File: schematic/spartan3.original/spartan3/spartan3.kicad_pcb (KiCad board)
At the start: 2 copper layers, 215.9 x 160 mm, 283 parts, among them U1_clk_select_0 SPFT_Sliding_Switch-dynacore, U2 XC3S250E-4TQG144C

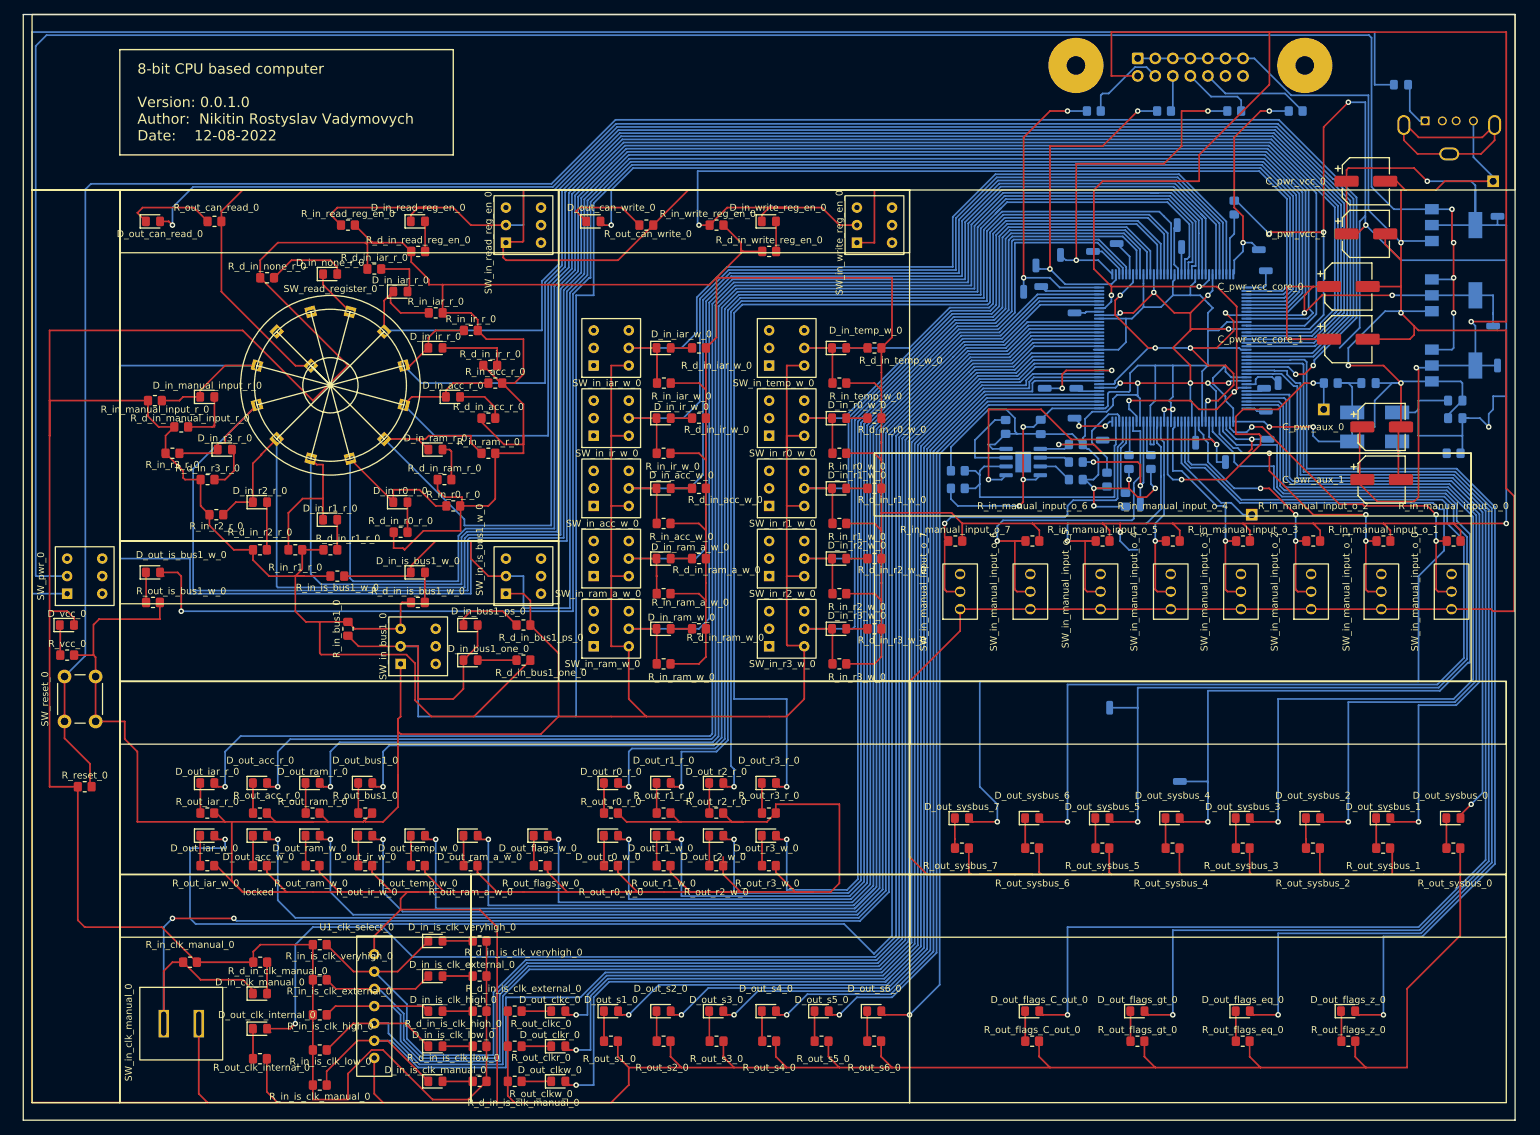
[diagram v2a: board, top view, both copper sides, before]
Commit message: Schematics/PCB layout updated. Gerber/Drill/BOM re-generated
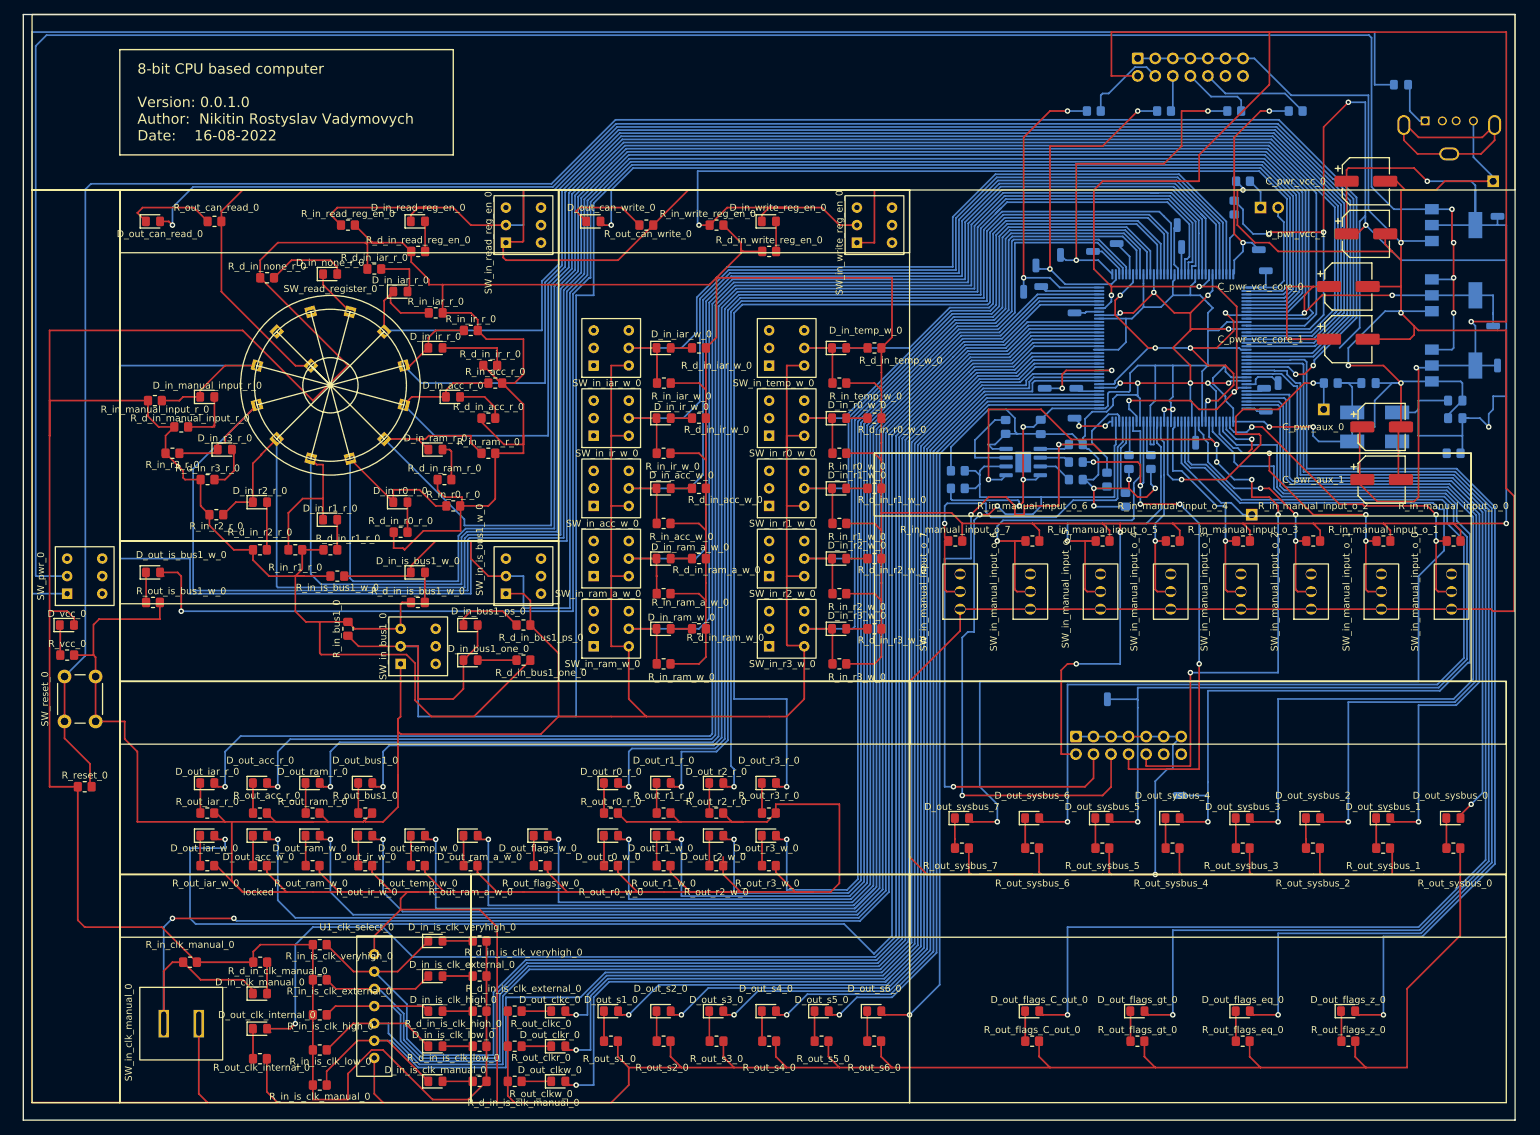
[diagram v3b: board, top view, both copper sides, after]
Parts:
- removed J_D0_DIN_0, J_eeprom_spi_clk_0, J_eeprom_spi_cs_n_0, J_eeprom_spi_din_0: Conn_01x01_Male, Connector_Wire:SolderWirePad_1x01_SMD_1x2mm
- added JP_SPI_Direct_PRG_0: Jumper_2_Bridged, Connector_PinHeader_2.54mm:PinHeader_1x02_P2.54mm_Vertical, B.Cu at (179.1, 27.9)
- added P_JTAG_FLASH_0: Xilinx_JTAG, Connector_IDC:IDC-Header_2x07_P2.54mm_Vertical, B.Cu at (152.3, 104.5)
- added R_PROG_B_0: 820R, Resistor_SMD:R_0805_2012Metric_Pad1.20x1.40mm_HandSolder, B.Cu at (176.5, 24.1)
- P_JTAG_FPGA_0: renamed from P_JTAG_0; footprint Connector_IDC:IDC-Header_2x07-1MP_P2.54mm_Latch_Vertical -> Connector_IDC:IDC-Header_2x07_P2.54mm_Vertical
- R_HSWAP_EN_0, R_M_0, R_VS_0, R_VS_1, R_VS_2: value 1K -> 10K
- R_eeprom_spi_clk_pulldown_0, R_eeprom_spi_clk_pullup_0: value 10K -> 100R
- X_clk_0: value XO91 -> FTO50,000MS7-3.3v
- moved J_INIT_B_0 2.03 mm to (167.4, 113.0)
- moved J_DOUT_BUSY_0 1.27 mm to (156.9, 99.1)
- renumbered U2 to U_FPGA_0
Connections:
- net VS0 renamed P70
- net VS2 renamed P67
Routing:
- net P39: track 43.7 -> 135.8 mm, vias 2 -> 4
- net CCLK: track 45.2 -> 124.0 mm, vias 0 -> 3
- net P44: track 55.7 -> 125.9 mm, vias 2 -> 6
- net GND: track 1928.7 -> 1997.9 mm, vias 11 -> 13
- net D0_DIN: track 24.2 -> 81.6 mm, vias 2 -> 5
- net VCC: track 1353.4 -> 1392.5 mm, vias 21 -> 22
- net P1: track 5.07 -> 21.8 mm
- net Net-(JP_SPI_Direct_PRG_0-Pad1): track 0.00 -> 4.45 mm
- net P69: track 51.4 -> 54.5 mm
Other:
- board text added: "8-bit CPU based computer Version: 0.0.1.0 Author: Nikitin Rostyslav Vadymovych Date: 16-08-2022"
- board text removed: "8-bit CPU based computer Version: 0.0.1.0 Author: Nikitin Rostyslav Vadymovych Date: 12-08-2022"
